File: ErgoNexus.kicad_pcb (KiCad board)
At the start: 2 copper layers, 172.1 x 137.2 mm, 110 parts, among them J7 Conn_01x02, J8 Conn_01x02, SW1 SW_Push, SW2 RotaryEncoder_Switch, SW3 SW_Push, SW4 RotaryEncoder_Switch, U1 SuperMini nRF52840, U2 SuperMini nRF52840

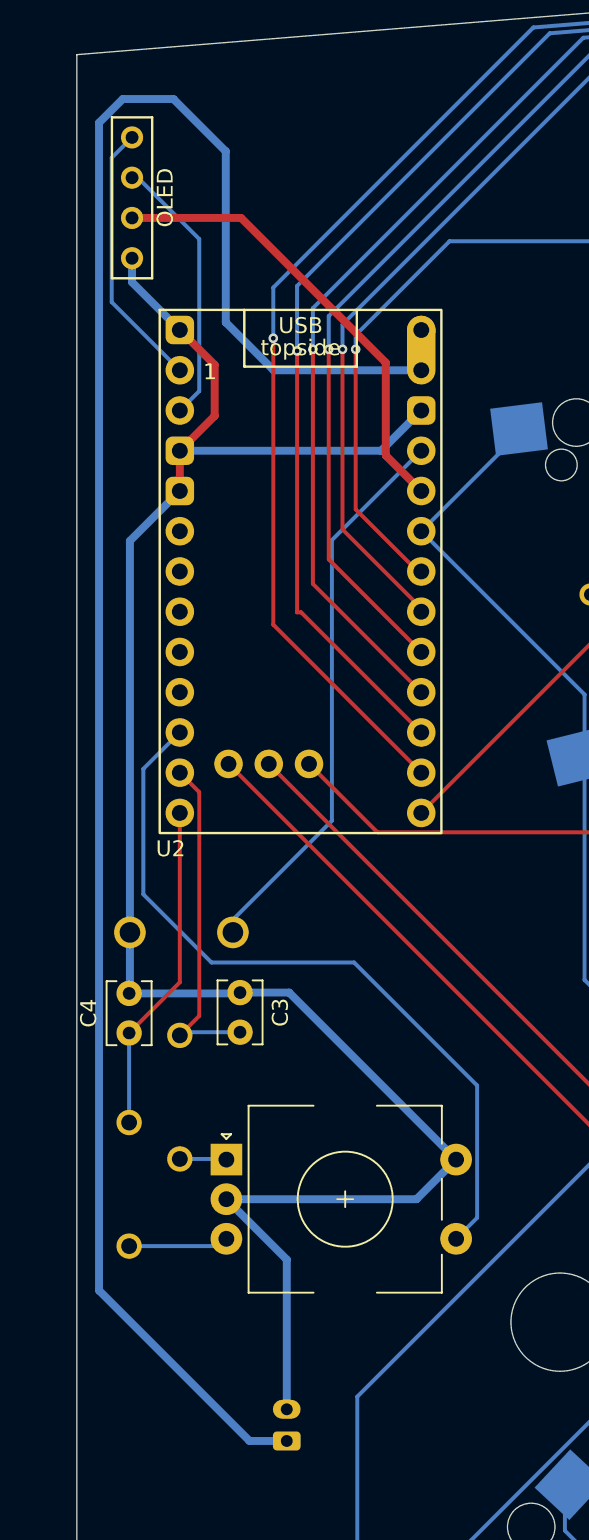
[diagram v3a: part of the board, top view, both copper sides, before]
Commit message: feat: 左手の回路図の配置を修正
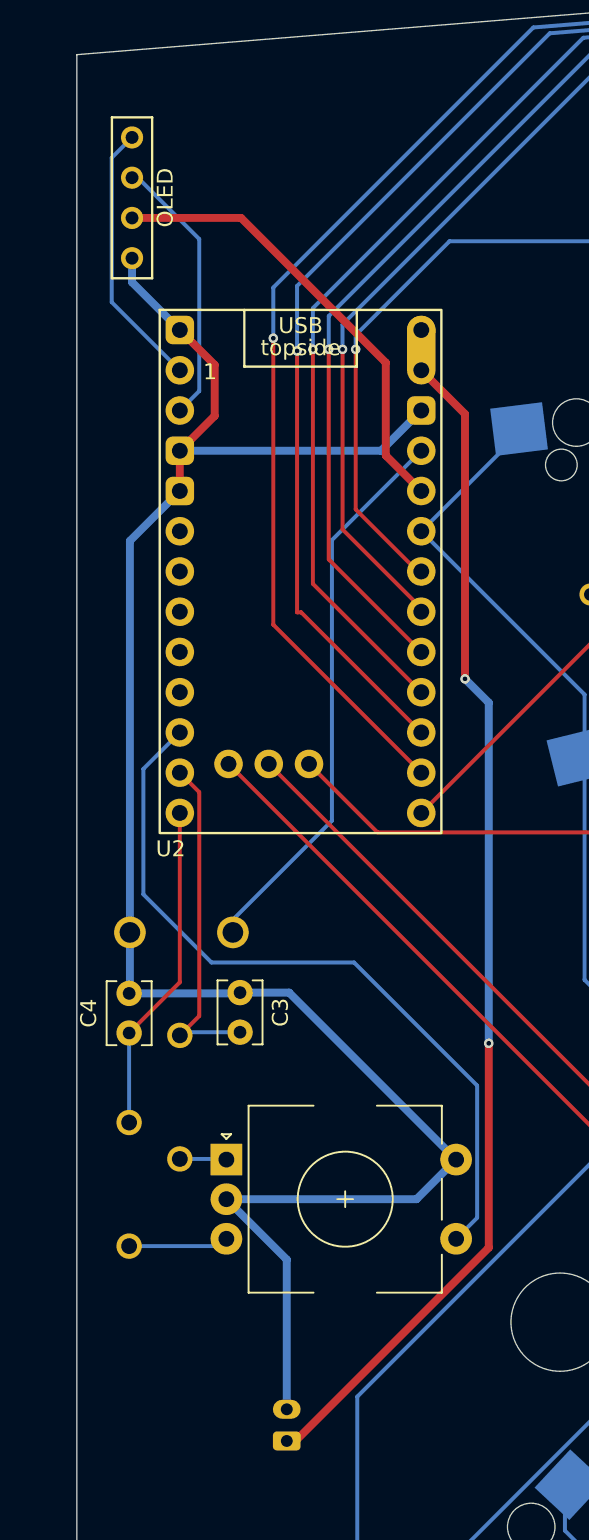
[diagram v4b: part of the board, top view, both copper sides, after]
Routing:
- net BAT_R: track 123.9 -> 74.9 mm, vias 0 -> 2
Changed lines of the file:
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@@
 	)
 	(segment
-		(start 235.785 74.479666)
-		(end 232.485 71.179666)
+		(start 250.885 107.779666)
+		(end 250.885 91.059666)
+		(width 0.5)
+		(layer "F.Cu")
+		(net 80)
+	)
+	(segment
+		(start 252.385 130.779666)
+		(end 252.385 143.679666)
+		(width 0.5)
+		(layer "F.Cu")
+		(net 80)
+	)
+	(segment
+		(start 250.885 91.059666)
+		(end 248.125 88.299666)
+		(width 0.5)
+		(layer "F.Cu")
+		(net 80)
+	)
+	(segment
+		(start 240.185 155.879666)
+		(end 239.635 155.879666)
+		(width 0.5)
+		(layer "F.Cu")
+		(net 80)
+	)
+	(segment
+		(start 252.385 143.679666)
+		(end 240.185 155.879666)
+		(width 0.5)
+		(layer "F.Cu")
+		(net 80)
+	)
+	(via
+		(at 252.385 130.779666)
+		(size 0.6)
+		(drill 0.3)
+		(layers "F.Cu" "B.Cu")
+		(net 80)
+	)
+	(via
+		(at 250.885 107.779666)
+		(size 0.6)
+		(drill 0.3)
+		(layers "F.Cu" "B.Cu")
+		(net 80)
+	)
+	(segment
+		(start 250.885 107.779666)
+		(end 252.385 109.279666)
 		(width 0.5)
 		(layer "B.Cu")
@@
 	)
 	(segment
-		(start 229.285 71.179666)
-		(end 227.785 72.679666)
+		(start 252.385 109.279666)
+		(end 252.385 130.779666)
 		(width 0.5)
 		(layer "B.Cu")
-		(net 80)
-	)
-	(segment
-		(start 232.485 71.179666)
-		(end 229.285 71.179666)
-		(width 0.5)
-		(layer "B.Cu")
-		(net 80)
-	)
-	(segment
-		(start 227.785 146.379666)
-		(end 237.285 155.879666)
-		(width 0.5)
-		(layer "B.Cu")
-		(net 80)
-	)
-	(segment
-		(start 235.785 85.279666)
-		(end 235.785 74.479666)
-		(width 0.5)
-		(layer "B.Cu")
-		(net 80)
-	)
-	(segment
-		(start 227.785 72.679666)
-		(end 227.785 146.379666)
-		(width 0.5)
-		(layer "B.Cu")
-		(net 80)
-	)
-	(segment
-		(start 238.805 88.299666)
-		(end 235.785 85.279666)
-		(width 0.5)
-		(layer "B.Cu")
-		(net 80)
-	)
-	(segment
-		(start 248.125 88.299666)
-		(end 238.805 88.299666)
-		(width 0.5)
-		(layer "B.Cu")
-		(net 80)
-	)
-	(segment
-		(start 237.285 155.879666)
-		(end 239.635 155.879666)
-		(width 0.5)
-		(layer "B.Cu")

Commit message: feat: 左手の配線完了
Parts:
- J8, SW1, SW3: moved to B.Cu
- R1: renamed from R2; moved to B.Cu
- R2: renamed from R1; moved to B.Cu
- moved U1 198.2 mm to (212.2, 102.2)
- moved K_L_41 181.6 mm to (208.1, 184.1), turned to -62 degrees
- moved D_L_41 167.4 mm to (200.7, 188.0), turned to -62 degrees
- moved K_L_11 158.6 mm to (190.7, 93.6), turned to -7.12 degrees
- moved K_L_42 154.7 mm to (195.7, 166.6), turned to -47 degrees
- moved K_L_21 151.0 mm to (186.9, 113.4), turned to -14 degrees
- moved D_L_42 146.7 mm to (190.3, 172.6), turned to -47 degrees
- moved K_L_31 139.3 mm to (180.9, 132.6), turned to -21 degrees
- moved K_L_12 136.5 mm to (172.6, 82.1), turned to -5 degrees
- moved K_L_22 132.1 mm to (169.7, 102.0), turned to -11.4 degrees
- moved J8 129.2 mm to (213.1, 155.9), turned to -90 degrees
- moved K_L_43 126.7 mm to (177.6, 153.6), turned to -25 degrees
- moved D_L_43 126.4 mm to (174.6, 161.4), turned to -25 degrees
- moved D_L_31 120.4 mm to (178.5, 140.5), turned to -21 degrees
- moved D_L_21 117.8 mm to (185.5, 121.6), turned to -14 degrees
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- renumbered C2 to C1, C1 to C2
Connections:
- C1 pad 1: Ro_B_L -> GND_L
- C1 pad 2: GND_L -> Ro_A_L
- C2 pad 1: GND_L -> Ro_B_L
- C2 pad 2: Ro_A_L -> GND_L
- R1 pad 1: Ro_B_L -> Ro_A_L
- R1 pad 2: Net-(R2-Pad2) -> Net-(R1-Pad2)
- R2 pad 1: Ro_A_L -> Ro_B_L
- R2 pad 2: Net-(R1-Pad2) -> Net-(R2-Pad2)
- U1 pad 10: RoSW_L -> Col6_L
- U1 pad 11: Ro_A_L -> Col7_L
- U1 pad 12: Ro_B_L -> Row1_L
- U1 pad 17: Col1_L -> unconnected-(U1-P0.31-LF-Pad17)
- U1 pad 18: Col2_L -> unconnected-(U1-P0.29-LF-Pad18)
- U1 pad 19: Col3_L -> unconnected-(U1-P0.02-LF-Pad19)
- U1 pad 20: Col4_L -> unconnected-(U1-P1.15-LF-Pad20)
- U1 pad 21: Col5_L -> unconnected-(U1-P1.13-LF-Pad21)
- U1 pad 22: Col6_L -> RoSW_L
- U1 pad 23: Col7_L -> Ro_A_L
- U1 pad 24: Row1_L -> Ro_B_L
- U1 pad 25: Row4_L -> Row2_L
- U1 pad 27: Row2_L -> Row4_L
- U1 pad 5: unconnected-(U1-P0.17-Pad5) -> Col1_L
- U1 pad 6: unconnected-(U1-P0.20-Pad6) -> Col2_L
- U1 pad 7: unconnected-(U1-P0.22-Pad7) -> Col3_L
- U1 pad 8: unconnected-(U1-P0.24-Pad8) -> Col4_L
- U1 pad 9: unconnected-(U1-P1.00-Pad9) -> Col5_L
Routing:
- net Row4_L: track 0.00 -> 231.2 mm
- net Col6_L: track 0.00 -> 216.4 mm, vias 0 -> 1
- net Col4_L: track 0.00 -> 215.7 mm, vias 0 -> 1
- net Col7_L: track 0.00 -> 207.9 mm, vias 0 -> 1
- net Col5_L: track 0.00 -> 194.4 mm, vias 0 -> 1
- net Row3_L: track 0.00 -> 192.8 mm
- net Col3_L: track 0.00 -> 192.1 mm, vias 0 -> 1
- net Col2_L: track 0.00 -> 169.5 mm, vias 0 -> 1
- net Row2_L: track 0.00 -> 152.1 mm
- net Col1_L: track 0.00 -> 142.0 mm
- net GND_L: track 0.00 -> 130.5 mm
- net Row1_L: track 0.00 -> 97.5 mm
- net BAT_L: track 0.00 -> 79.2 mm, vias 0 -> 1
- net RoSW_L: track 0.00 -> 34.2 mm
- net RST_L: track 0.00 -> 33.4 mm
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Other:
- board size 172.1 x 137.2 mm -> 344.2 x 137.2 mm
- board text added: "Left-Back"
- board text added: "Left-Front"

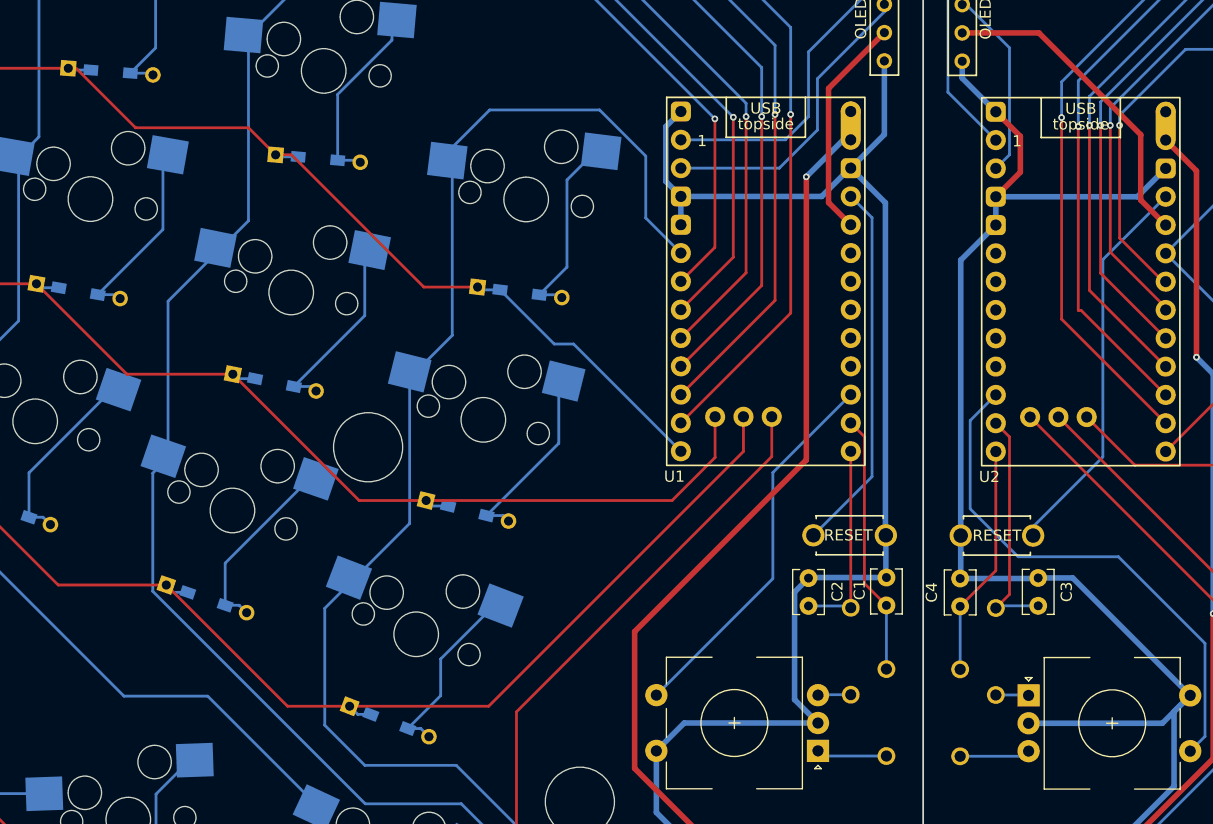
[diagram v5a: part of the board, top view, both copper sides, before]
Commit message: fix: 左右のキーボードを合わせることで、jlcpcb向けデータが正しく出力されるように
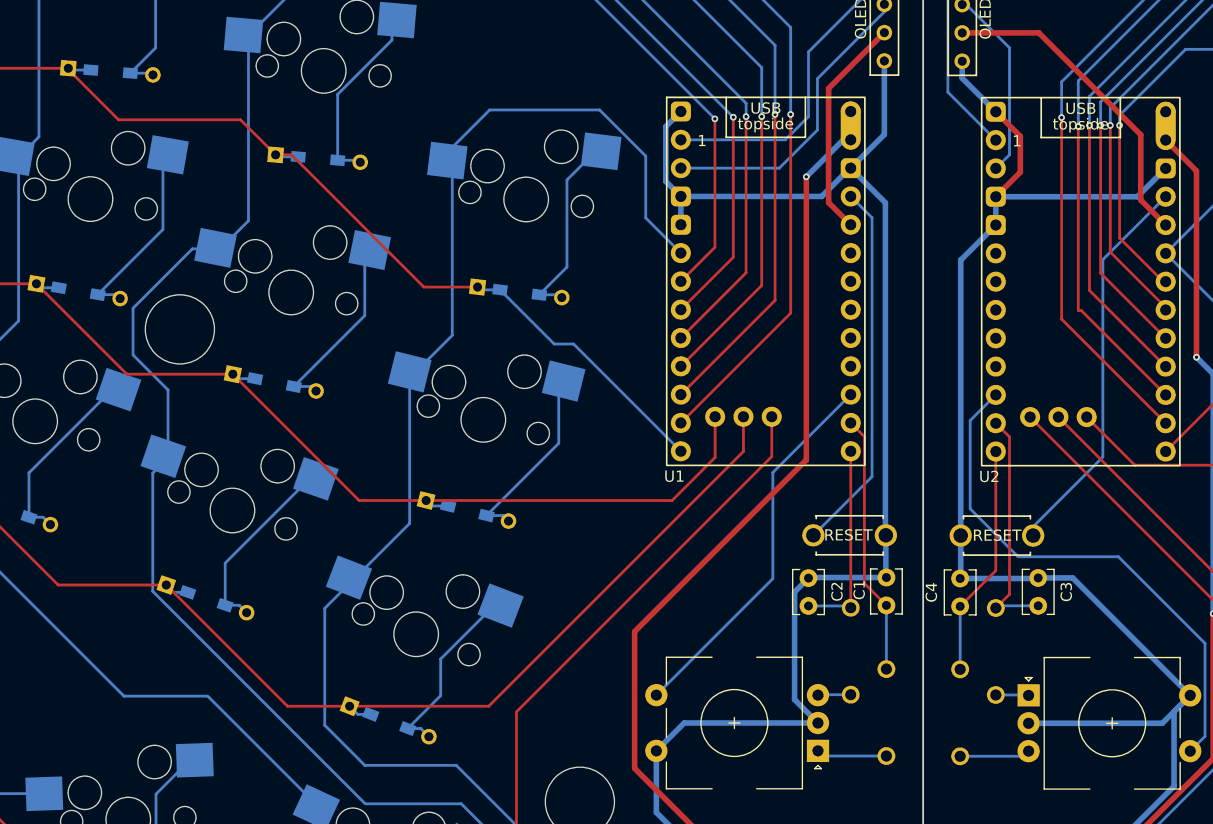
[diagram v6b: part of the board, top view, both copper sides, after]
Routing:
- net Col2_L: track 169.5 -> 173.6 mm
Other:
- outline, holes or cut-outs redrawn

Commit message: feat: フィレットとVカットの追加
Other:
- board size 344.2 x 137.2 mm -> 343.9 x 136.5 mm

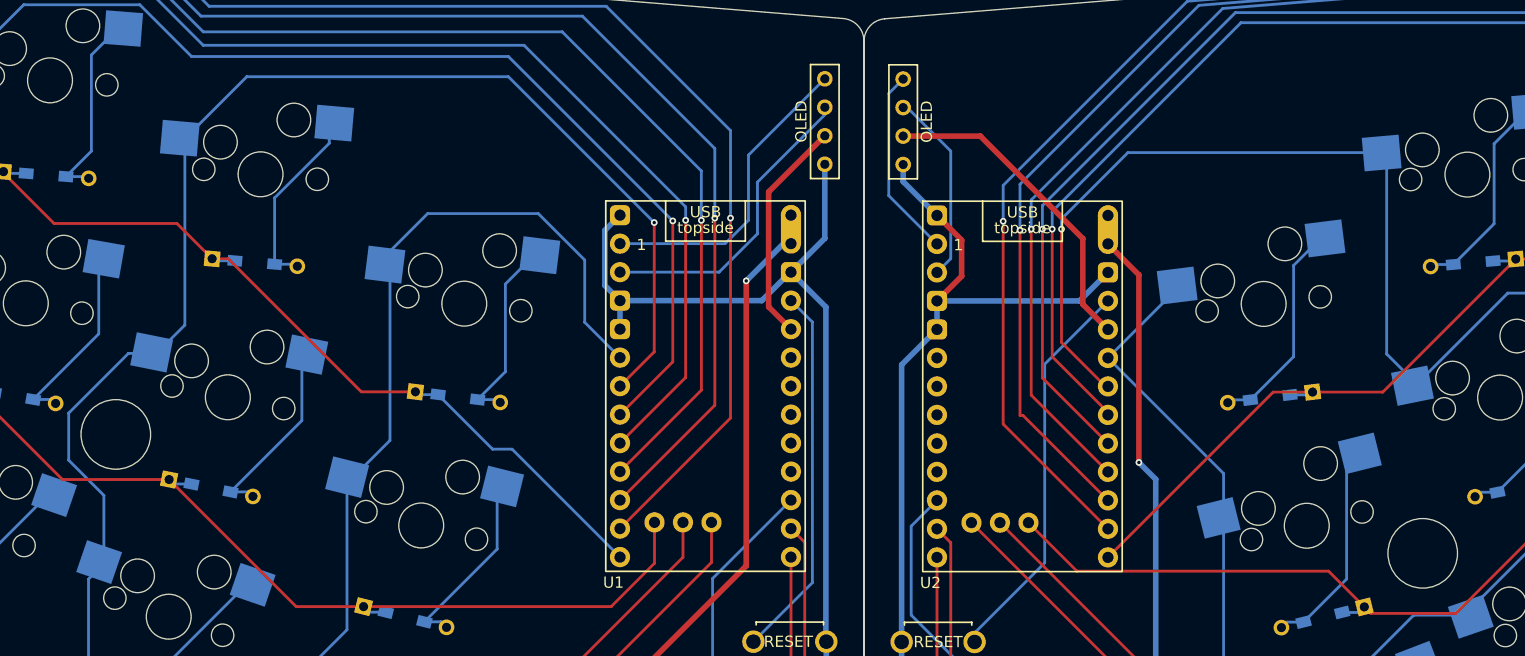
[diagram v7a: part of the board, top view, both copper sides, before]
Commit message: fix: ネジ穴を調整
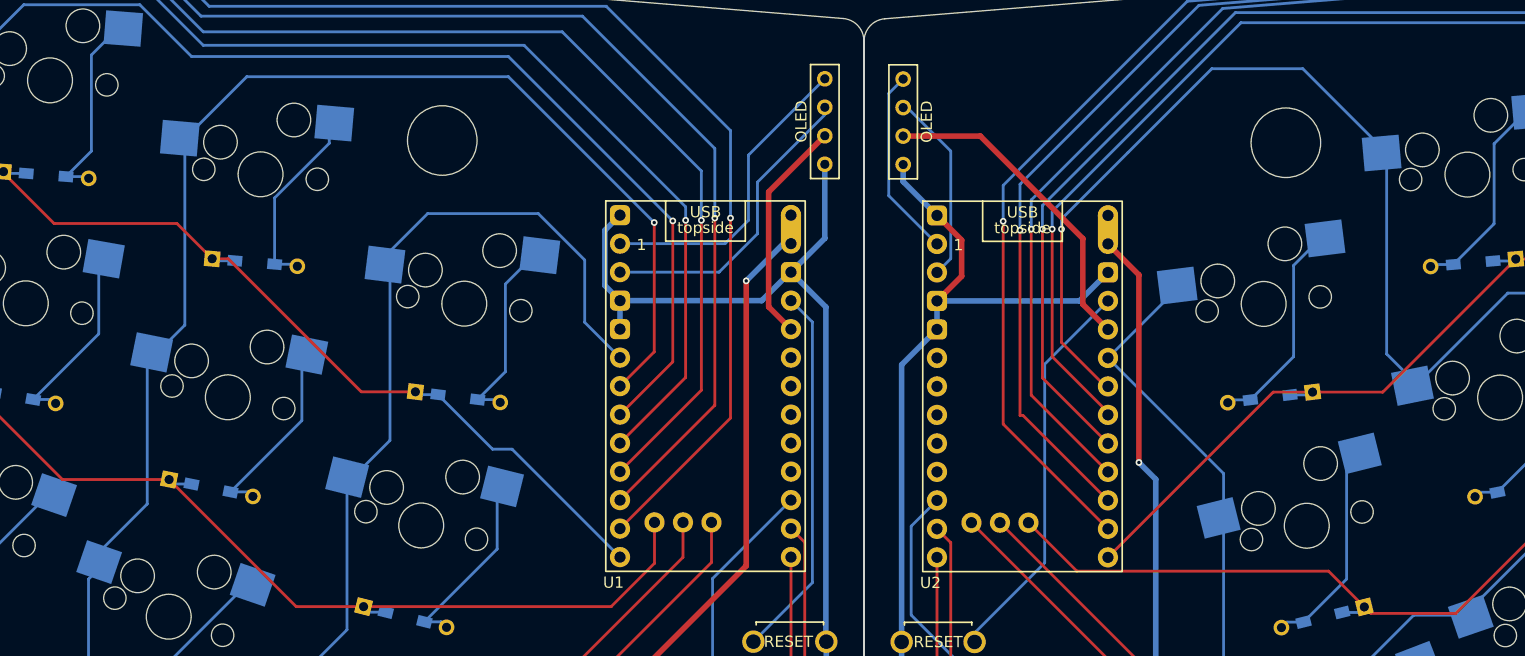
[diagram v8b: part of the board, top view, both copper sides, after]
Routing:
- net Col2_R: track 184.4 -> 190.6 mm
- net Col2_L: track 173.6 -> 169.5 mm
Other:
- outline, holes or cut-outs redrawn
